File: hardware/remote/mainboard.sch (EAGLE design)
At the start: 4 parts, among them U1 ATMEGA328P_VQFNVQFN, U2 RFM69HCW

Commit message: Scehamtic work
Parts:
- added C1, C2: 100n, SparkFun-Passives:CAP0603-CAP
- added J1: AVR_SPI_PRG_6PTH, SparkFun-Connectors:AVR_SPI_PRG_6PTH
- added R1: 10k, SparkFun-Passives:RESISTOR0603-RES
- added R2: 50k, SparkFun-Passives:RESISTOR0603-RES
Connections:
- new net GND: BAT1.-, C1.2, C2.2, J1.6, U1.GND@1, U1.GND@2, U1.GND@PAD, U2.ANT, U2.GND@1, U2.GND@2
- new net MISO: J1.1, U1.PB4(MISO), U2.MOSI
- new net MOSI: J1.4, U1.PB3(MOSI/OC2), U2.MISO
- new net N$1: BAT1.+, S1.2
- new net N$2: J1.5, R1.2, U1.PC6(/RESET)
- new net N$6: R2.2, U1.PD4(XCK/T0), U2.NSS
- new net N$8: U1.PD2(INT0), U2.DIO0
- new net SCK: J1.3, U1.PB5(SCK), U2.SCK
- new net VCC: C1.1, C2.1, J1.2, R1.1, R2.1, S1.1, U1.AVCC, U1.VCC, U2.3.3V

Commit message: Preliminary schematic design
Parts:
- added C3: 10u, SparkFun-Passives:CAP1206
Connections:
- new net N$3: C2.2, U2.GND@2
- net GND: now also C3.2; no longer C2.2, U2.ANT, U2.GND@2
- net VCC: now also C3.1
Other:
- moved on the sheet: BAT1, S1
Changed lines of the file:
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@@
 <part name="GND4" library="SparkFun-Aesthetics" deviceset="GND" device=""/>
 <part name="R2" library="SparkFun-Passives" deviceset="RESISTOR" device="0603-RES" value="50k"/>
+<part name="C3" library="SparkFun-Passives" deviceset="CAP" device="1206" value="10u"/>
 </parts>
 <sheets>
@@
 <instance part="U1" gate="G$1" x="53.34" y="45.72"/>
 <instance part="U2" gate="G$1" x="152.4" y="63.5"/>
-<instance part="BAT1" gate="G$1" x="30.48" y="114.3"/>
-<instance part="S1" gate="G$1" x="15.24" y="114.3"/>
-<instance part="SUPPLY1" gate="G$1" x="7.62" y="116.84"/>
-<instance part="GND1" gate="1" x="38.1" y="104.14"/>
+<instance part="BAT1" gate="G$1" x="30.48" y="124.46"/>
+<instance part="S1" gate="G$1" x="15.24" y="124.46"/>
+<instance part="SUPPLY1" gate="G$1" x="5.08" y="127"/>
+<instance part="GND1" gate="1" x="38.1" y="106.68"/>
 <instance part="SUPPLY2" gate="G$1" x="10.16" y="78.74"/>
 <instance part="J1" gate="G$1" x="50.8" y="91.44"/>
@@
 <instance part="GND4" gate="1" x="170.18" y="48.26"/>
 <instance part="R2" gate="G$1" x="116.84" y="68.58" rot="R270"/>
+<instance part="C3" gate="G$1" x="7.62" y="116.84"/>
 </instances>
 <busses>
@@
 <segment>
 <pinref part="SUPPLY1" gate="G$1" pin="VCC"/>
-<wire x1="7.62" y1="116.84" x2="7.62" y2="114.3" width="0.1524" layer="91"/>
+<wire x1="5.08" y1="127" x2="5.08" y2="124.46" width="0.1524" layer="91"/>
 <pinref part="S1" gate="G$1" pin="1"/>
-<wire x1="7.62" y1="114.3" x2="10.16" y2="114.3" width="0.1524" layer="91"/>
+<wire x1="5.08" y1="124.46" x2="7.62" y2="124.46" width="0.1524" layer="91"/>
+<pinref part="C3" gate="G$1" pin="1"/>
+<wire x1="7.62" y1="124.46" x2="10.16" y2="124.46" width="0.1524" layer="91"/>
+<wire x1="7.62" y1="121.92" x2="7.62" y2="124.46" width="0.1524" layer="91"/>
+<junction x="7.62" y="124.46"/>
 </segment>
 <segment>
@@
 <pinref part="S1" gate="G$1" pin="2"/>
 <pinref part="BAT1" gate="G$1" pin="+"/>
-<wire x1="20.32" y1="114.3" x2="25.4" y2="114.3" width="0.1524" layer="91"/>
+<wire x1="20.32" y1="124.46" x2="25.4" y2="124.46" width="0.1524" layer="91"/>
 </segment>
 </net>
@@
 <pinref part="BAT1" gate="G$1" pin="-"/>
 <pinref part="GND1" gate="1" pin="GND"/>
-<wire x1="35.56" y1="114.3" x2="38.1" y2="114.3" width="0.1524" layer="91"/>
-<wire x1="38.1" y1="114.3" x2="38.1" y2="106.68" width="0.1524" layer="91"/>
+<wire x1="35.56" y1="124.46" x2="38.1" y2="124.46" width="0.1524" layer="91"/>
+<wire x1="38.1" y1="124.46" x2="38.1" y2="111.76" width="0.1524" layer="91"/>
+<pinref part="C3" gate="G$1" pin="2"/>
+<wire x1="38.1" y1="111.76" x2="38.1" y2="109.22" width="0.1524" layer="91"/>
+<wire x1="7.62" y1="114.3" x2="7.62" y2="111.76" width="0.1524" layer="91"/>
+<wire x1="7.62" y1="111.76" x2="38.1" y2="111.76" width="0.1524" layer="91"/>
+<junction x="38.1" y="111.76"/>
 </segment>
 <segment>
@@
 <pinref part="GND4" gate="1" pin="GND"/>
 <wire x1="170.18" y1="50.8" x2="170.18" y2="53.34" width="0.1524" layer="91"/>
-<pinref part="U2" gate="G$1" pin="GND@2"/>
-<wire x1="170.18" y1="53.34" x2="170.18" y2="55.88" width="0.1524" layer="91"/>
-<wire x1="170.18" y1="55.88" x2="170.18" y2="58.42" width="0.1524" layer="91"/>
-<wire x1="170.18" y1="58.42" x2="167.64" y2="58.42" width="0.1524" layer="91"/>
-<pinref part="U2" gate="G$1" pin="ANT"/>
-<wire x1="167.64" y1="55.88" x2="170.18" y2="55.88" width="0.1524" layer="91"/>
-<junction x="170.18" y="55.88"/>
 <pinref part="U2" gate="G$1" pin="GND@1"/>
 <wire x1="167.64" y1="53.34" x2="170.18" y2="53.34" width="0.1524" layer="91"/>
-<junction x="170.18" y="53.34"/>
-<pinref part="C2" gate="G$1" pin="2"/>
-<wire x1="172.72" y1="63.5" x2="172.72" y2="58.42" width="0.1524" layer="91"/>
-<wire x1="172.72" y1="58.42" x2="170.18" y2="58.42" width="0.1524" layer="91"/>
-<junction x="170.18" y="58.42"/>
 </segment>
 </net>
@@
 </segment>
 </net>
+<net name="N$3" class="0">
+<segment>
+<pinref part="U2" gate="G$1" pin="GND@2"/>
+<pinref part="C2" gate="G$1" pin="2"/>
+<wire x1="172.72" y1="63.5" x2="172.72" y2="58.42" width="0.1524" layer="91"/>
+<wire x1="172.72" y1="58.42" x2="167.64" y2="58.42" width="0.1524" layer="91"/>
+</segment>
+</net>

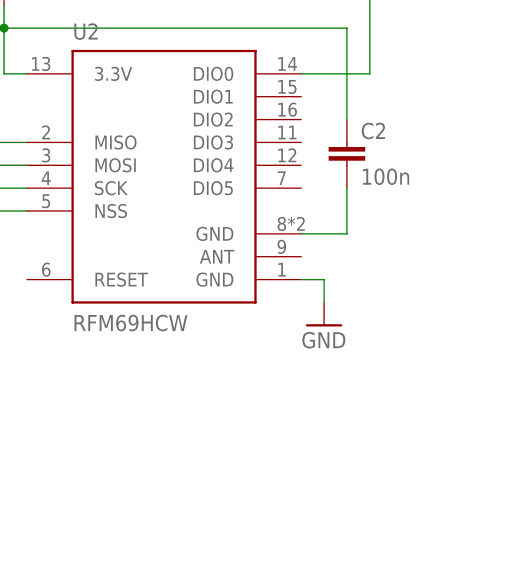
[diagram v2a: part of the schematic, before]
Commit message: PCB component placement and antenna connector
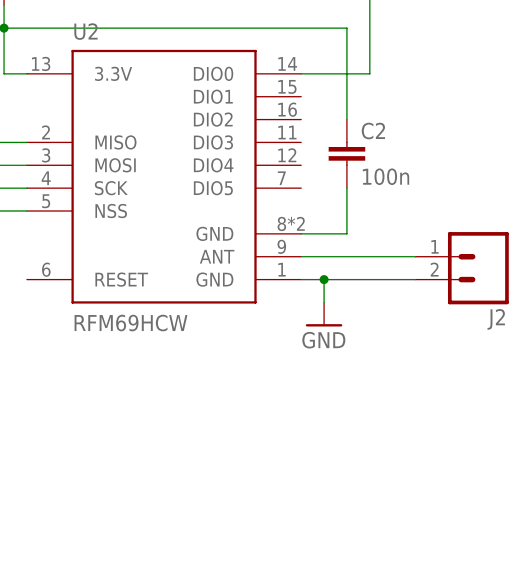
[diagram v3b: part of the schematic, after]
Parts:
- added J2: (no value), SparkFun-Connectors:M02PTH
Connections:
- new net N$4: J2.1, U2.ANT
- net GND: now also J2.2
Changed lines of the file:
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@@
 <part name="R2" library="SparkFun-Passives" deviceset="RESISTOR" device="0603-RES" value="50k"/>
 <part name="C3" library="SparkFun-Passives" deviceset="CAP" device="1206" value="10u"/>
+<part name="J2" library="SparkFun-Connectors" deviceset="M02" device="PTH"/>
 </parts>
 <sheets>
@@
 <instance part="R2" gate="G$1" x="116.84" y="68.58" rot="R270"/>
 <instance part="C3" gate="G$1" x="7.62" y="116.84"/>
+<instance part="J2" gate="G$1" x="187.96" y="55.88" rot="R180"/>
 </instances>
 <busses>
@@
 <pinref part="U2" gate="G$1" pin="GND@1"/>
 <wire x1="167.64" y1="53.34" x2="170.18" y2="53.34" width="0.1524" layer="91"/>
+<pinref part="J2" gate="G$1" pin="2"/>
+<wire x1="180.34" y1="53.34" x2="170.18" y2="53.34" width="0.1524" layer="91"/>
+<junction x="170.18" y="53.34"/>
 </segment>
 </net>
@@
 </segment>
 </net>
+<net name="N$4" class="0">
+<segment>
+<pinref part="J2" gate="G$1" pin="1"/>
+<pinref part="U2" gate="G$1" pin="ANT"/>
+<wire x1="180.34" y1="55.88" x2="167.64" y2="55.88" width="0.1524" layer="91"/>
+</segment>
+</net>

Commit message: Preliminary PCB design
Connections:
- removed net N$3: C2.2, U2.GND@2
- net GND: now also C2.2, U2.GND@2
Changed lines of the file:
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@@
 <part name="GND1" library="SparkFun-Aesthetics" deviceset="GND" device=""/>
 <part name="SUPPLY2" library="SparkFun-Aesthetics" deviceset="VCC" device=""/>
-<part name="J1" library="SparkFun-Connectors" deviceset="AVR_SPI_PRG_6" device="PTH"/>
+<part name="J1" library="SparkFun-Connectors" deviceset="AVR_SPI_PRG_6" device="PTH" value=""/>
 <part name="R1" library="SparkFun-Passives" deviceset="RESISTOR" device="0603-RES" value="10k"/>
 <part name="GND2" library="SparkFun-Aesthetics" deviceset="GND" device=""/>
@@
 <wire x1="180.34" y1="53.34" x2="170.18" y2="53.34" width="0.1524" layer="91"/>
 <junction x="170.18" y="53.34"/>
+<pinref part="U2" gate="G$1" pin="GND@2"/>
+<pinref part="C2" gate="G$1" pin="2"/>
+<wire x1="172.72" y1="63.5" x2="172.72" y2="58.42" width="0.1524" layer="91"/>
+<wire x1="172.72" y1="58.42" x2="170.18" y2="58.42" width="0.1524" layer="91"/>
+<wire x1="170.18" y1="58.42" x2="167.64" y2="58.42" width="0.1524" layer="91"/>
+<wire x1="170.18" y1="58.42" x2="170.18" y2="53.34" width="0.1524" layer="91"/>
+<junction x="170.18" y="58.42"/>
 </segment>
 </net>
@@
 </segment>
 </net>
-<net name="N$3" class="0">
-<segment>
-<pinref part="U2" gate="G$1" pin="GND@2"/>
-<pinref part="C2" gate="G$1" pin="2"/>
-<wire x1="172.72" y1="63.5" x2="172.72" y2="58.42" width="0.1524" layer="91"/>
-<wire x1="172.72" y1="58.42" x2="167.64" y2="58.42" width="0.1524" layer="91"/>
-</segment>
-</net>

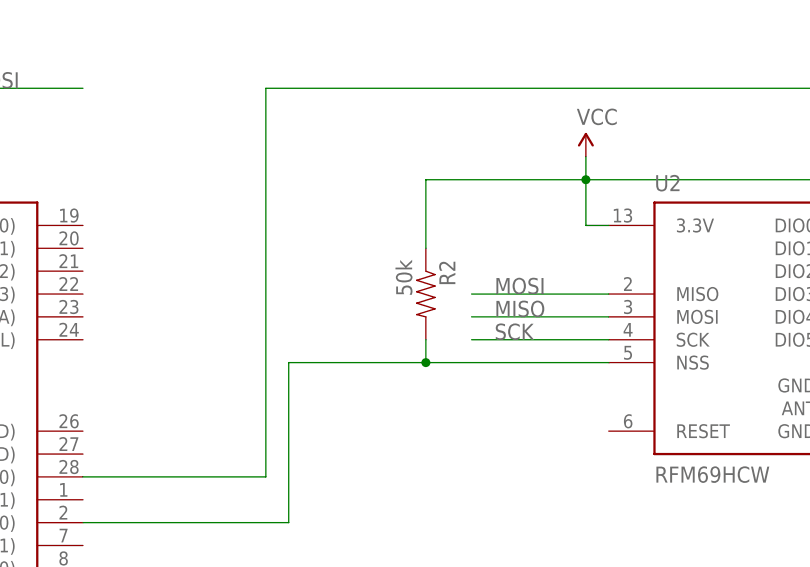
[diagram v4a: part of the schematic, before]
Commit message: Added BOM and modified resistor value
Remote
* Added detailed BOM with digikey part numbers.
* Changed R2 from 50k to 47k as 47k is a much more common value.
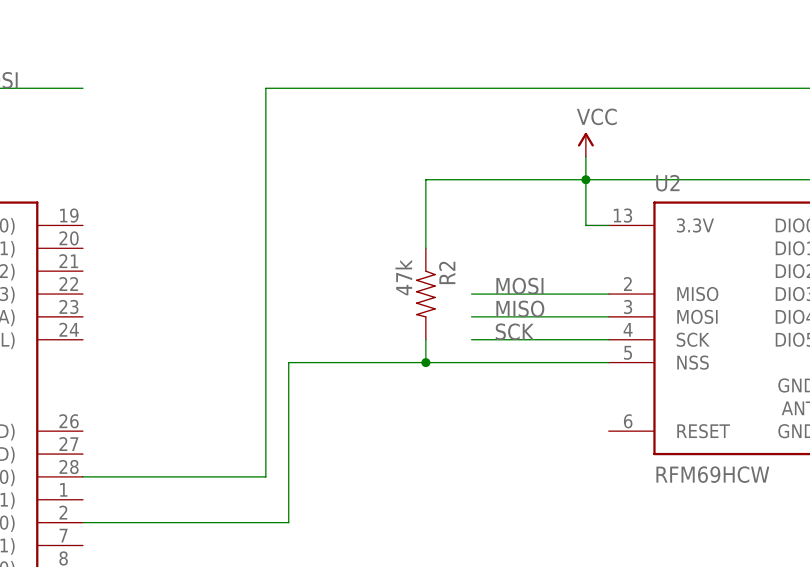
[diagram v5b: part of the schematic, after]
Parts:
- R2: value 50k -> 47k
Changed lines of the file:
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@@
 <part name="SUPPLY4" library="SparkFun-Aesthetics" deviceset="VCC" device=""/>
 <part name="GND4" library="SparkFun-Aesthetics" deviceset="GND" device=""/>
-<part name="R2" library="SparkFun-Passives" deviceset="RESISTOR" device="0603-RES" value="50k"/>
+<part name="R2" library="SparkFun-Passives" deviceset="RESISTOR" device="0603-RES" value="47k"/>
 <part name="C3" library="SparkFun-Passives" deviceset="CAP" device="1206" value="10u"/>
 <part name="J2" library="SparkFun-Connectors" deviceset="M02" device="PTH"/>

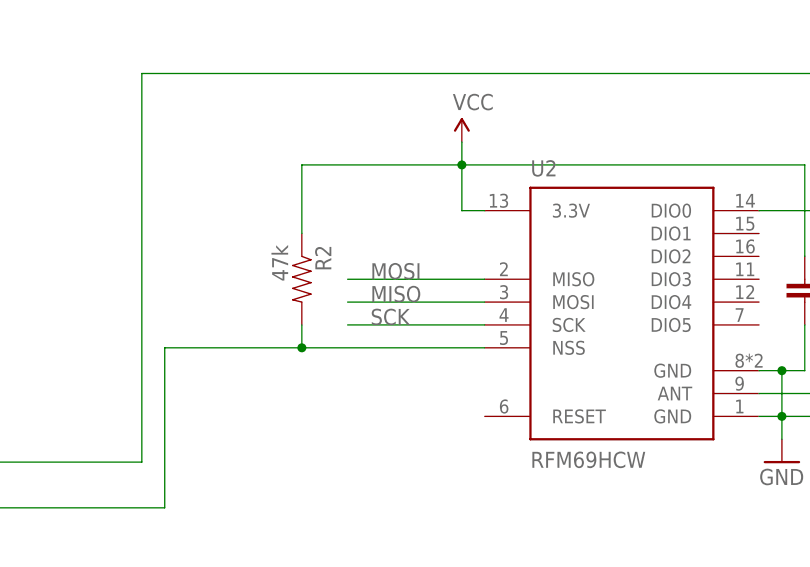
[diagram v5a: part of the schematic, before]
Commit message: Fixed SPI mismatch
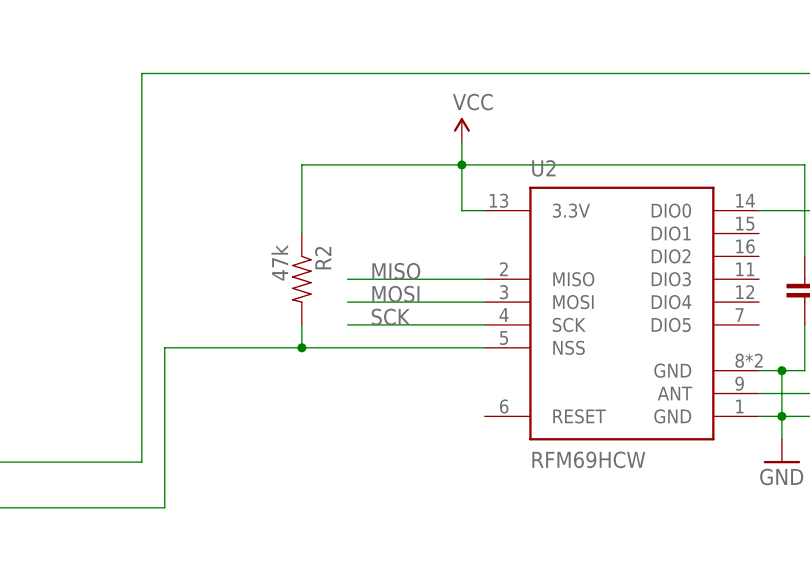
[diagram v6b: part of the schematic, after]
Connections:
- net MISO: now also U2.MISO; no longer U2.MOSI
- net MOSI: now also U2.MOSI; no longer U2.MISO
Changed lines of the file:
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@@
-</segment>
-<segment>
-<pinref part="U2" gate="G$1" pin="MOSI"/>
-<wire x1="137.16" y1="66.04" x2="121.92" y2="66.04" width="0.1524" layer="91"/>
-<label x="124.46" y="66.04" size="1.778" layer="95"/>
 </segment>
 <segment>
@@
 <wire x1="43.18" y1="93.98" x2="25.4" y2="93.98" width="0.1524" layer="91"/>
 <label x="27.94" y="93.98" size="1.778" layer="95"/>
+</segment>
+<segment>
+<pinref part="U2" gate="G$1" pin="MISO"/>
+<wire x1="137.16" y1="68.58" x2="121.92" y2="68.58" width="0.1524" layer="91"/>
+<label x="124.46" y="68.58" size="1.778" layer="95"/>
 </segment>
 </net>
@@
 </segment>
 <segment>
-<pinref part="U2" gate="G$1" pin="MISO"/>
-<wire x1="137.16" y1="68.58" x2="121.92" y2="68.58" width="0.1524" layer="91"/>
-<label x="124.46" y="68.58" size="1.778" layer="95"/>
-</segment>
-<segment>
 <pinref part="J1" gate="G$1" pin="4"/>
 <wire x1="60.96" y1="91.44" x2="78.74" y2="91.44" width="0.1524" layer="91"/>
 <label x="66.04" y="91.44" size="1.778" layer="95"/>
+</segment>
+<segment>
+<pinref part="U2" gate="G$1" pin="MOSI"/>
+<wire x1="137.16" y1="66.04" x2="121.92" y2="66.04" width="0.1524" layer="91"/>
+<label x="124.46" y="66.04" size="1.778" layer="95"/>
 </segment>
 </net>
@@
 </sheet>
 </sheets>
+<errors>
+</errors>
 </schematic>
 </drawing>

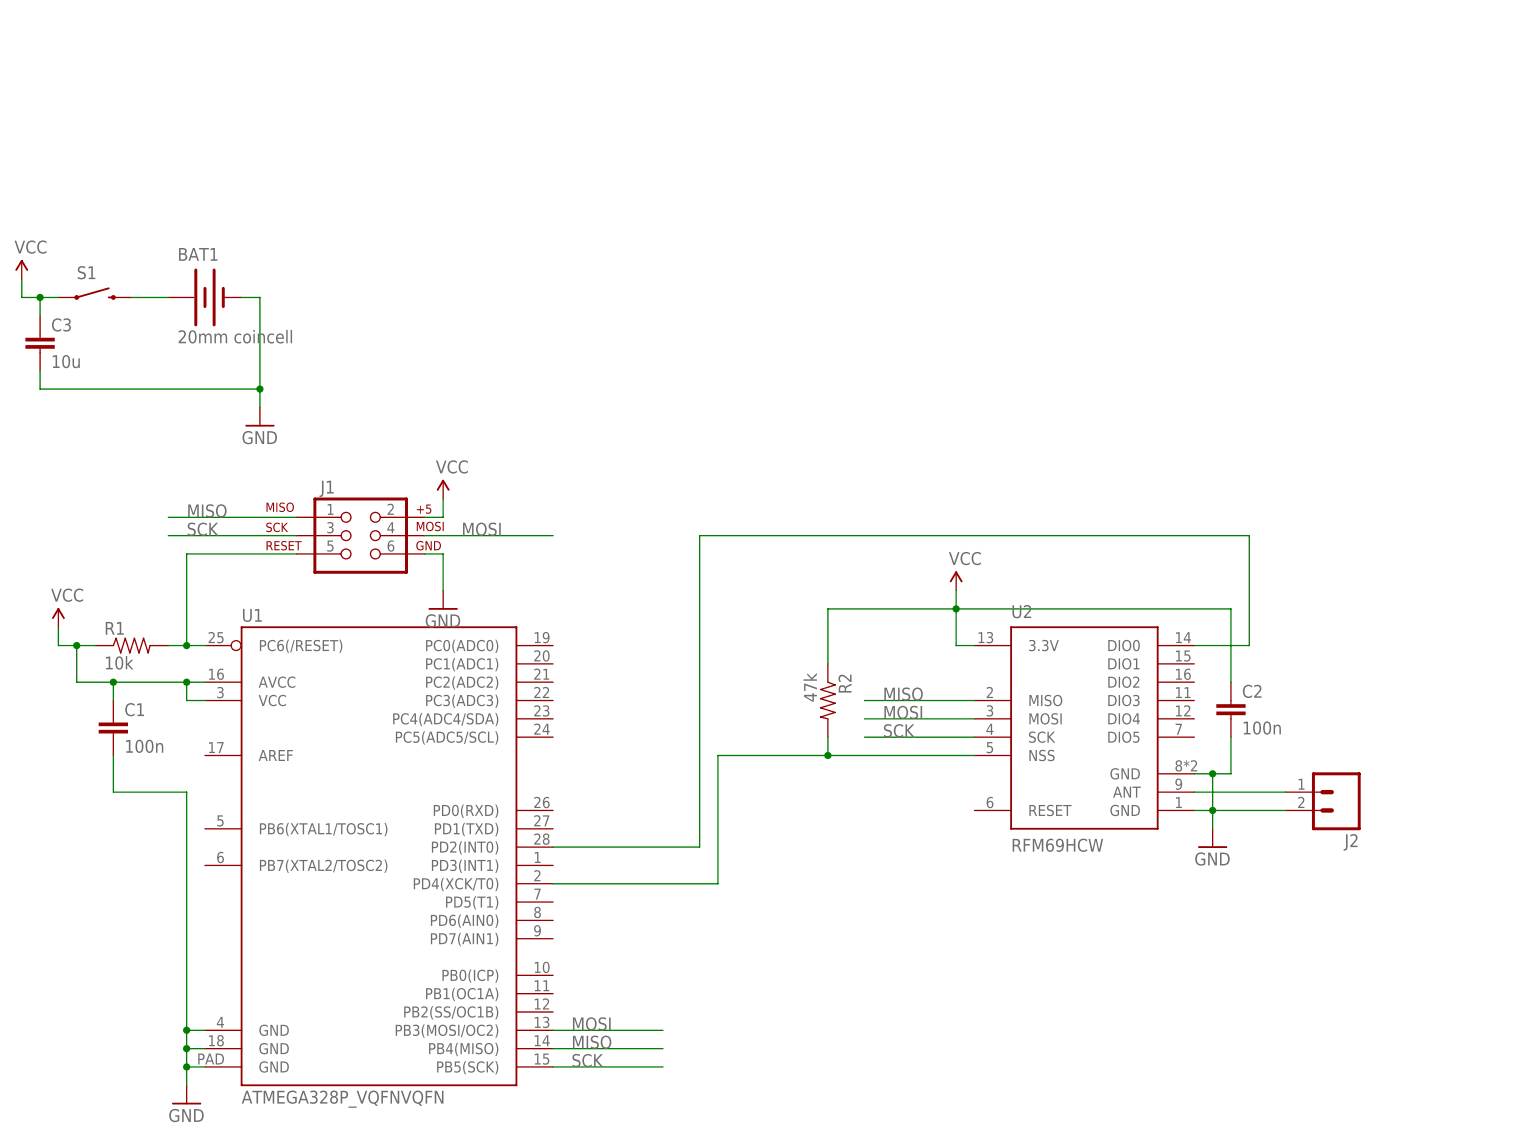
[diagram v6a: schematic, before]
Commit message: Added frames
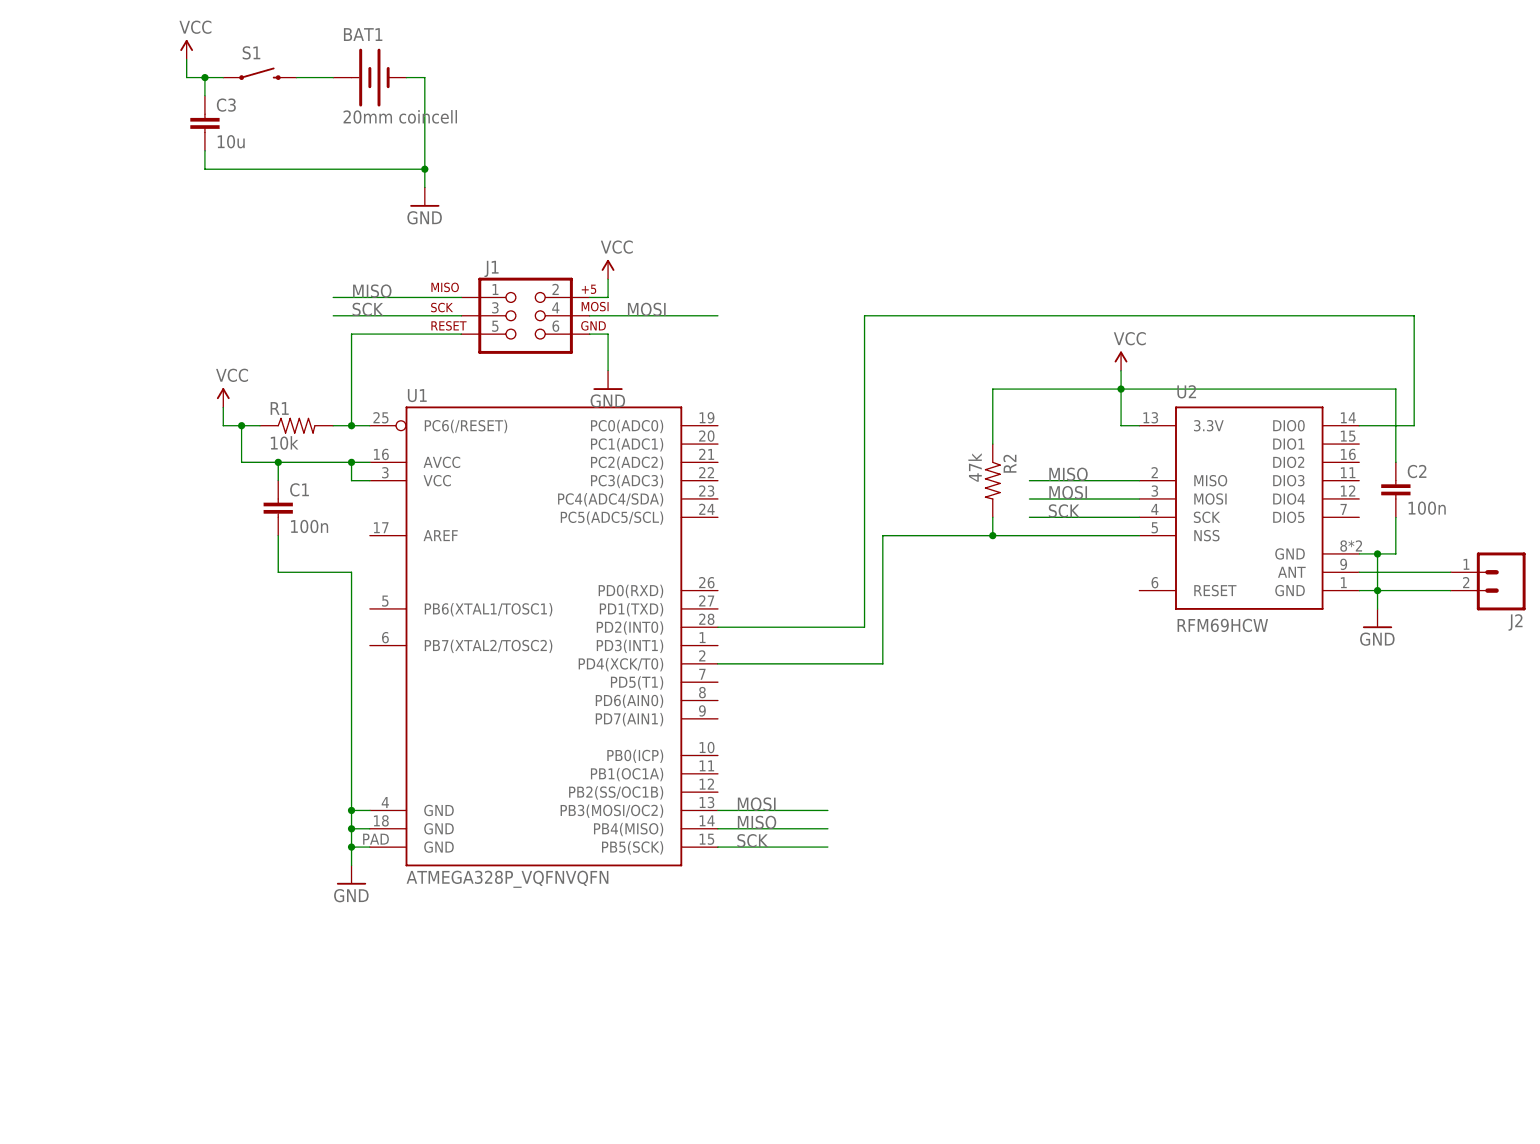
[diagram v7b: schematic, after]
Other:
- moved on the sheet: BAT1, C1, C2, C3, J1, J2, R1, R2, S1, U1, U2
